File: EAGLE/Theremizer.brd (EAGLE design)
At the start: 160 x 100 mm, 166 parts, among them IC1 AS3320, IC2 NE5532N, IC3 TL072D, IC4 NE5532N, J1 3x2 M, J2 1x6 M, J3 AUDIO_JACK_TRS_0.25"_PTH_RA, J4 POWER_JACK, J5 AUDIO_JACK_TRS_0.25"_PTH_RA, Q1 PMV45EN2R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

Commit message: Redid layout, hopefully better
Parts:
- removed R49: 0, rcl:R0805
- removed TP2: TPPAD1-13, testpad:P1-13
- added JP10, JP11, JP12: (no value), jumper:JP1
- R20, R8: value 0 -> 15k
- R34: device pot:PT-10 -> pot:B64Y
- moved R60 263.9 mm to (61.0, 78.7), turned to 180 degrees
- moved H2 179.9 mm to (36.8, -59.7)
- moved H3 159.5 mm to (19.1, -62.2)
- moved H1 151.8 mm to (30.5, -61.0)
- moved C45 140.6 mm to (14.0, 91.4), turned to 180 degrees
- moved C42 136.6 mm to (14.0, 88.9), turned to 180 degrees
- moved C44 123.0 mm to (27.9, 91.4), turned to 270 degrees
- moved IC3 122.4 mm to (21.6, 90.2), turned to 270 degrees
- moved C43 117.9 mm to (30.5, 91.4)
- moved R45 99.9 mm to (34.3, 74.9), turned to 90 degrees
- moved C36 98.3 mm to (52.7, 78.7)
- moved H4 93.7 mm to (25.4, -62.2)
- moved C39 92.6 mm to (55.2, 78.7)
- moved R55 87.9 mm to (61.0, 88.9), turned to 0 degrees
- moved J5 86.3 mm to (82.5, 124.5), turned to 270 degrees
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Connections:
- new net N$75: C40.2, C41.2, U5.4
- new net N$77: R43.E, R8.1
- new net N$78: R20.1, R44.E
- net +15V: now also JP10.2; no longer R20.2
- net +5V: now also JP12.2, R20.2, R8.2; no longer R43.E, R44.E, R8.1
- net -15V: now also JP11.1; no longer R49.2
- net 5VEXT: now also JP12.1; no longer R8.2, TP2.TP
- net N$55: now also JP10.1; no longer R20.1
- net N$56: now also JP11.2; no longer R49.1
- net THEREMIN_OUT: no longer C40.2, C41.2, U5.4
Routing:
- net GND: track 906.1 -> 0.00 mm, vias 4 -> 0
- net +9V: track 401.7 -> 0.00 mm, vias 7 -> 0
- net -15V: track 285.8 -> 0.00 mm, vias 2 -> 0
- net +5V: track 223.3 -> 0.00 mm, vias 6 -> 0
- net +15V: track 182.4 -> 0.00 mm, vias 5 -> 0
- net RES_CV: track 174.7 -> 0.00 mm, vias 6 -> 0
- net FILTER_OUTPUT: track 142.6 -> 0.00 mm, vias 5 -> 0
- net N$55: track 123.1 -> 0.00 mm
- net N$52: track 122.0 -> 0.00 mm, vias 1 -> 0
- net N$19: track 116.8 -> 0.00 mm, vias 3 -> 0
- net N$56: track 112.1 -> 0.00 mm, vias 1 -> 0
- net N$50: track 111.1 -> 0.00 mm, vias 2 -> 0
- net OUTPUT: track 101.2 -> 0.00 mm
- net N$74: track 96.9 -> 0.00 mm, vias 2 -> 0
- net FREQ_CV: track 94.3 -> 0.00 mm, vias 8 -> 0
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- added copper zone on layer 1, net GND
- removed copper zone on layer 1, net GND1
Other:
- board size 160 x 100 mm -> 102.9 x 124.5 mm

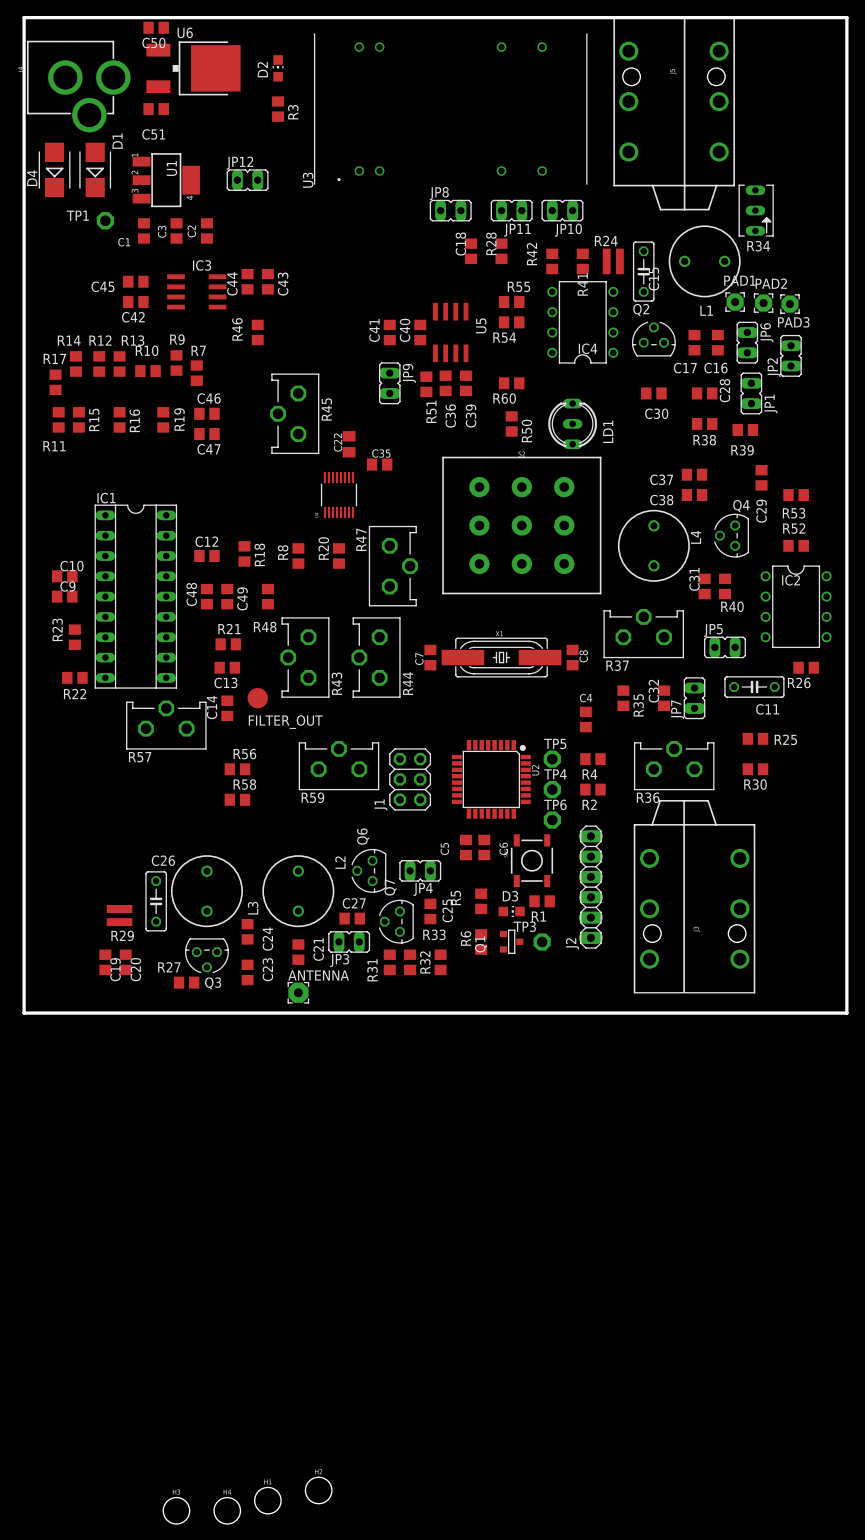
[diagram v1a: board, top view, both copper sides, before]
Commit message: Board laid out by hand, still needs vias
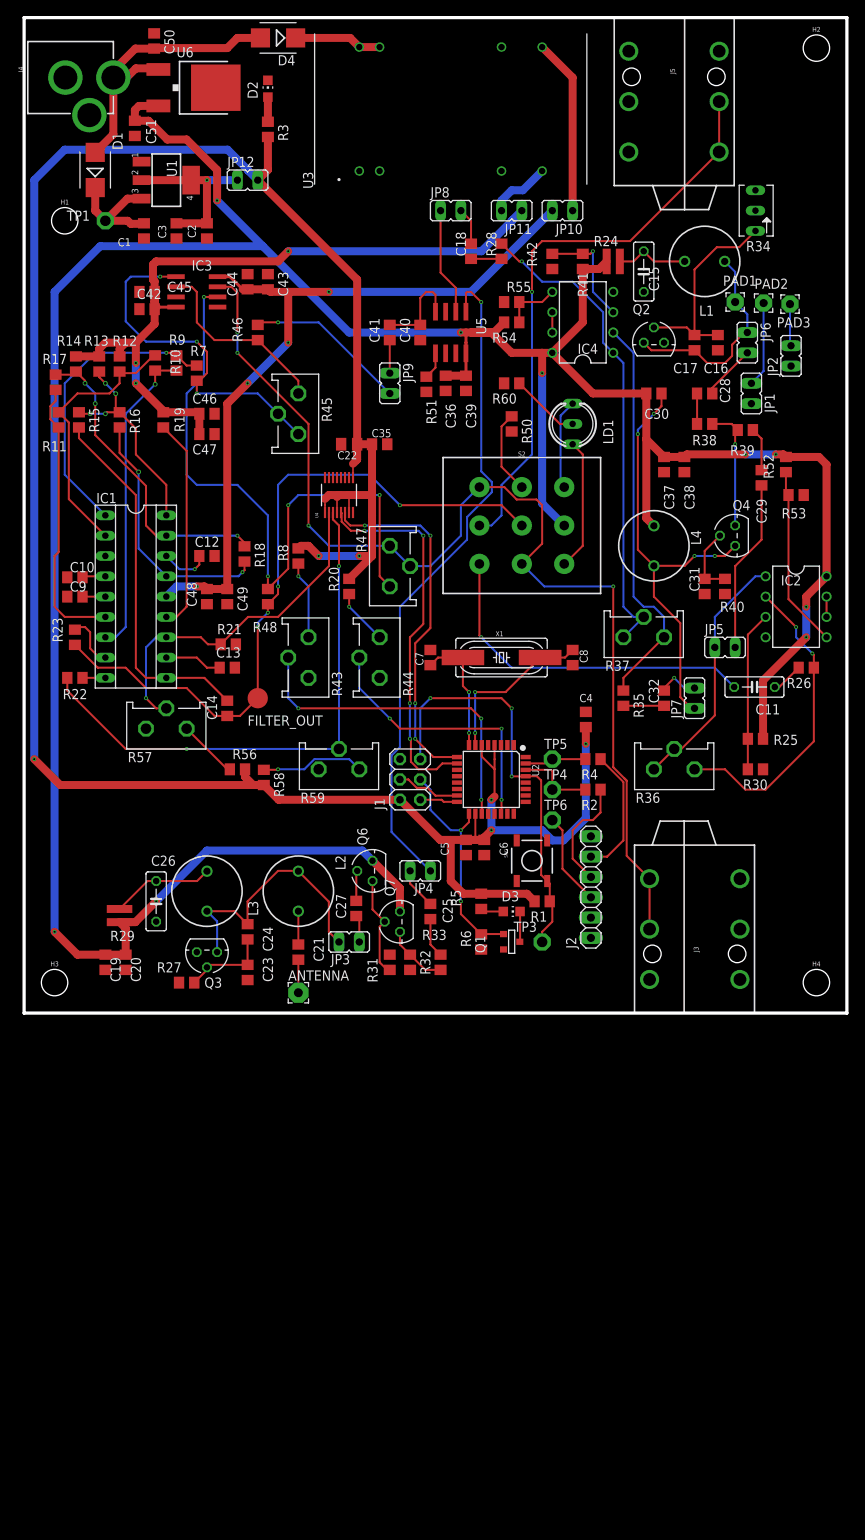
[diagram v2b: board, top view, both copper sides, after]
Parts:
- C32: value 10u -> 0.1u
- moved H2 190.8 mm to (99.1, 120.7)
- moved H1 162.0 mm to (5.08, 99.1)
- moved H4 98.9 mm to (99.1, 3.81)
- moved H3 67.8 mm to (3.81, 3.81)
- moved D4 32.5 mm to (31.8, 121.9), turned to 180 degrees
- moved R52 10.2 mm to (95.2, 68.6), turned to 90 degrees
- moved R58 4.33 mm to (30.0, 29.5), turned to 270 degrees
- moved C38 4.02 mm to (82.5, 68.6), turned to 270 degrees
- moved R20 4.02 mm to (40.6, 53.3)
- moved C37 4.02 mm to (80.0, 68.6), turned to 270 degrees
- moved C51 3.60 mm to (13.8, 110.6), turned to 270 degrees
- moved D2 2.84 mm to (30.5, 115.6)
- moved R3 2.84 mm to (30.5, 110.5)
- moved C35 2.54 mm to (44.5, 71.1)
- moved R12 2.54 mm to (11.9, 81.2)
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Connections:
- removed net N$47: J5.SLEEVE-NORM
- net GND: now also J5.SLEEVE-NORM, U4.10, U4.11
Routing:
- net +9V: track 0.00 -> 380.7 mm, vias 0 -> 9
- net +5V: track 0.00 -> 318.3 mm, vias 0 -> 6
- net OUTPUT: track 0.00 -> 140.2 mm, vias 0 -> 4
- net +15V: track 0.00 -> 95.4 mm, vias 0 -> 4
- net -15V: track 0.00 -> 91.9 mm, vias 0 -> 3
- net FILTER_OUTPUT: track 0.00 -> 88.8 mm, vias 0 -> 4
- net N$24: track 0.00 -> 83.7 mm, vias 0 -> 1
- net N$52: track 0.00 -> 81.7 mm, vias 0 -> 4
- net N$37: track 0.00 -> 72.7 mm, vias 0 -> 1
- net RES_CV: track 0.00 -> 68.5 mm, vias 0 -> 2
- net N$49: track 0.00 -> 60.8 mm, vias 0 -> 1
- net N$45: track 0.00 -> 54.9 mm, vias 0 -> 4
- net !RESET: track 0.00 -> 52.5 mm, vias 0 -> 3
- net N$48: track 0.00 -> 50.2 mm
- net PWM_B: track 0.00 -> 47.6 mm, vias 0 -> 4
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
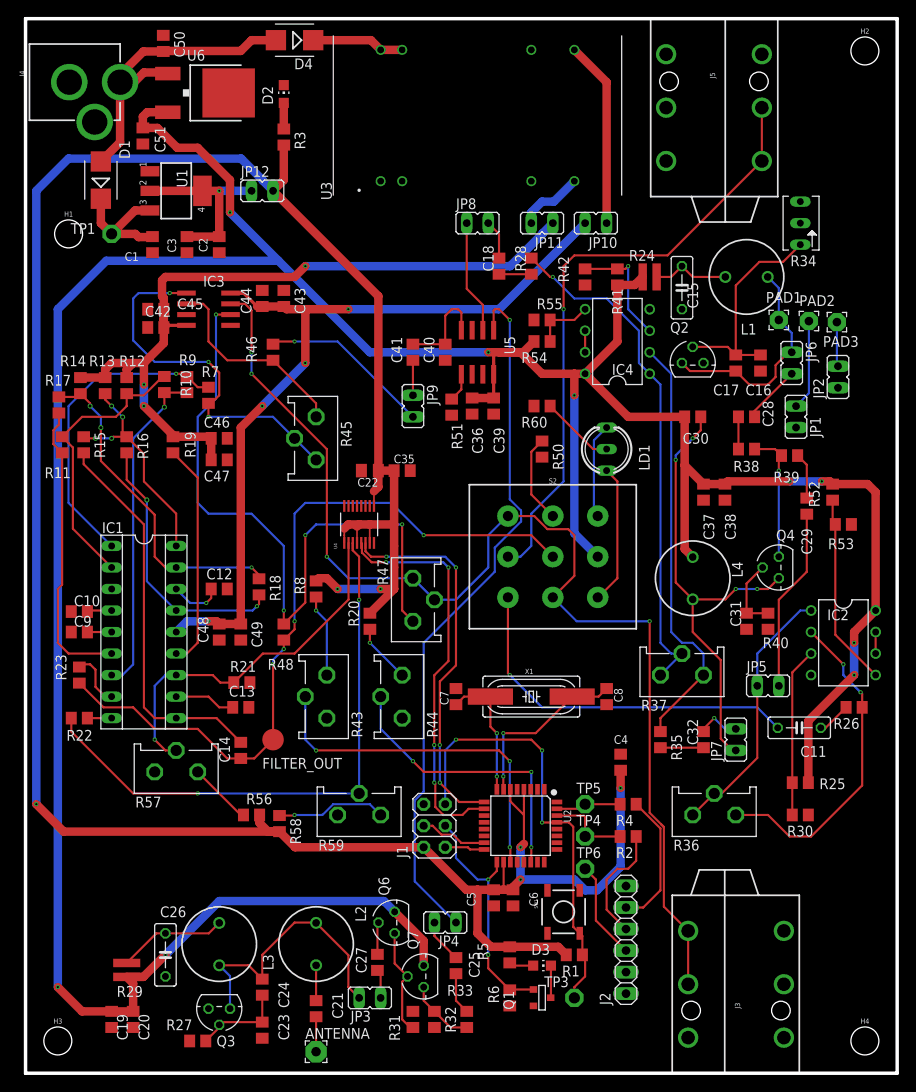
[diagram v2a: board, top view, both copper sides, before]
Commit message: Now with 1000000x more vias
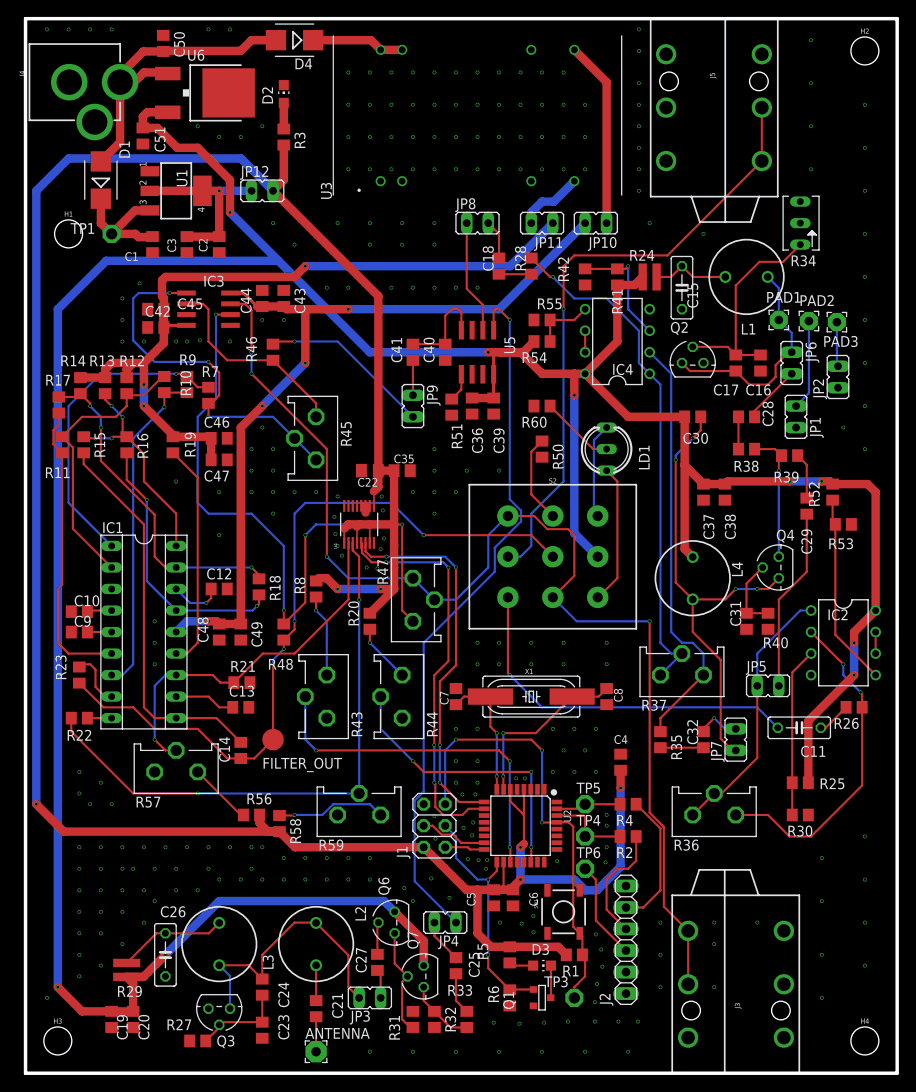
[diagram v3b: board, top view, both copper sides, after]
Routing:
- net GND: track 0.00 -> 0.79 mm, vias 0 -> 281

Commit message: Final Schematic/Board Layout
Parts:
- added D5: M7, diode:SMA
- D1: device diode:SMB -> diode:SMA
- D4: value M7 -> MBRA340T3; device diode:SMB -> diode:SMA
- R36, R37, R43, R44, R45, R47, R57, R59: device pot:ECP10P -> pot:B64Y
- moved C50 6.00 mm to (15.6, 115.6), turned to 180 degrees
- moved D4 1.27 mm to (31.8, 120.7)
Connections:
- new net N$47: C50.1, D5.C, U6.1
- net N$51: now also D5.A; no longer C50.1, U6.1
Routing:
- net RES_CV: track 68.5 -> 52.0 mm
- net N$65: track 13.0 -> 5.09 mm
- net N$32: track 7.50 -> 15.1 mm, vias 0 -> 1
- net N$47: track 0.00 -> 6.63 mm
- net N$77: track 9.74 -> 14.8 mm
- net N$40: track 39.1 -> 44.1 mm
- net N$19: track 24.0 -> 29.1 mm
- net N$78: track 6.98 -> 11.3 mm
- net OUTPUT: track 140.2 -> 143.3 mm
- net N$52: track 81.7 -> 84.0 mm
- net FREQ_CV: track 43.9 -> 45.5 mm
- net N$51: track 37.4 -> 36.4 mm, vias 0 -> 1
- net N$48: track 50.2 -> 51.3 mm
- net N$50: track 44.0 -> 45.0 mm
- net GND: track 0.79 -> 0.00 mm, vias 281 -> 283
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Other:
- board text added: "/Users/andrewforsman/Desktop/Theremizer_logo.bmp"
- board text added: "Rev. 00"
- board text added: "Team 18"

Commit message: Final Digikey BOM
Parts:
- C22: device rcl:C0805K -> rcl:C0805
- C27: value 200p -> 220p
- C5: value 100n -> 0.1u
- D4: value MBRA340T3 -> M7
- R36: value 100k -> 500k

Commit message: Connected airwire from RES_CV nodes
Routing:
- net RES_CV: track 52.0 -> 72.1 mm
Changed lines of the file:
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@@
 <layer number="21" name="tPlace" color="7" fill="1" visible="yes" active="yes"/>
 <layer number="22" name="bPlace" color="7" fill="1" visible="yes" active="yes"/>
-<layer number="23" name="tOrigins" color="15" fill="1" visible="no" active="yes"/>
+<layer number="23" name="tOrigins" color="15" fill="1" visible="yes" active="yes"/>
 <layer number="24" name="bOrigins" color="15" fill="1" visible="yes" active="yes"/>
-<layer number="25" name="tNames" color="7" fill="1" visible="no" active="yes"/>
+<layer number="25" name="tNames" color="7" fill="1" visible="yes" active="yes"/>
 <layer number="26" name="bNames" color="7" fill="1" visible="yes" active="yes"/>
 <layer number="27" name="tValues" color="7" fill="1" visible="no" active="yes"/>
@@
 <layer number="37" name="tTest" color="7" fill="1" visible="no" active="yes"/>
 <layer number="38" name="bTest" color="7" fill="1" visible="no" active="yes"/>
-<layer number="39" name="tKeepout" color="4" fill="11" visible="no" active="yes"/>
+<layer number="39" name="tKeepout" color="4" fill="11" visible="yes" active="yes"/>
 <layer number="40" name="bKeepout" color="1" fill="11" visible="yes" active="yes"/>
-<layer number="41" name="tRestrict" color="4" fill="10" visible="no" active="yes"/>
+<layer number="41" name="tRestrict" color="4" fill="10" visible="yes" active="yes"/>
 <layer number="42" name="bRestrict" color="1" fill="10" visible="yes" active="yes"/>
 <layer number="43" name="vRestrict" color="2" fill="10" visible="no" active="yes"/>
@@
 <layer number="49" name="Reference" color="7" fill="1" visible="no" active="yes"/>
 <layer number="50" name="dxf" color="12" fill="1" visible="no" active="no"/>
-<layer number="51" name="tDocu" color="7" fill="1" visible="no" active="yes"/>
+<layer number="51" name="tDocu" color="7" fill="1" visible="yes" active="yes"/>
 <layer number="52" name="bDocu" color="7" fill="1" visible="yes" active="yes"/>
 <layer number="53" name="tGND_GNDA" color="7" fill="1" visible="no" active="no"/>
@@
 </element>
 <element name="R10" library="rcl" library_urn="urn:adsk.eagle:library:334" package="R0805" package3d_urn="urn:adsk.eagle:package:23553/2" value="91K" x="16.383" y="81.28" smashed="yes" rot="R90">
-<attribute name="NAME" x="19.558" y="79.883" size="1.27" layer="25" rot="R90"/>
+<attribute name="NAME" x="17.78" y="84.836" size="1.27" layer="25" rot="R180"/>
 <attribute name="POPULARITY" value="85" x="247.523" y="-91.44" size="1.778" layer="27" display="off"/>
 <attribute name="SPICEPREFIX" value="R" x="247.523" y="-91.44" size="1.778" layer="27" display="off"/>
@@
 <wire x1="38.608" y1="61.722" x2="38.608" y2="62.57416875" width="0.254" layer="1"/>
 <wire x1="39.37" y1="55.88" x2="39.37" y2="60.96" width="0.254" layer="1"/>
-<wire x1="20.32" y1="33.02" x2="39.37" y2="30.48" width="0" layer="19" extent="1-1"/>
+<wire x1="39.37" y1="30.48" x2="36.83" y2="33.02" width="0.254" layer="1"/>
+<wire x1="36.83" y1="33.02" x2="20.32" y2="33.02" width="0.254" layer="1"/>
 </signal>
 <signal name="N$8">

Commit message: Buncha random things, added .png of logo
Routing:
- net N$65: track 5.09 -> 6.89 mm
- net RES_CV: vias 2 -> 1
